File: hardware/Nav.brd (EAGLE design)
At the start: 47 x 40.5 mm, 52 parts

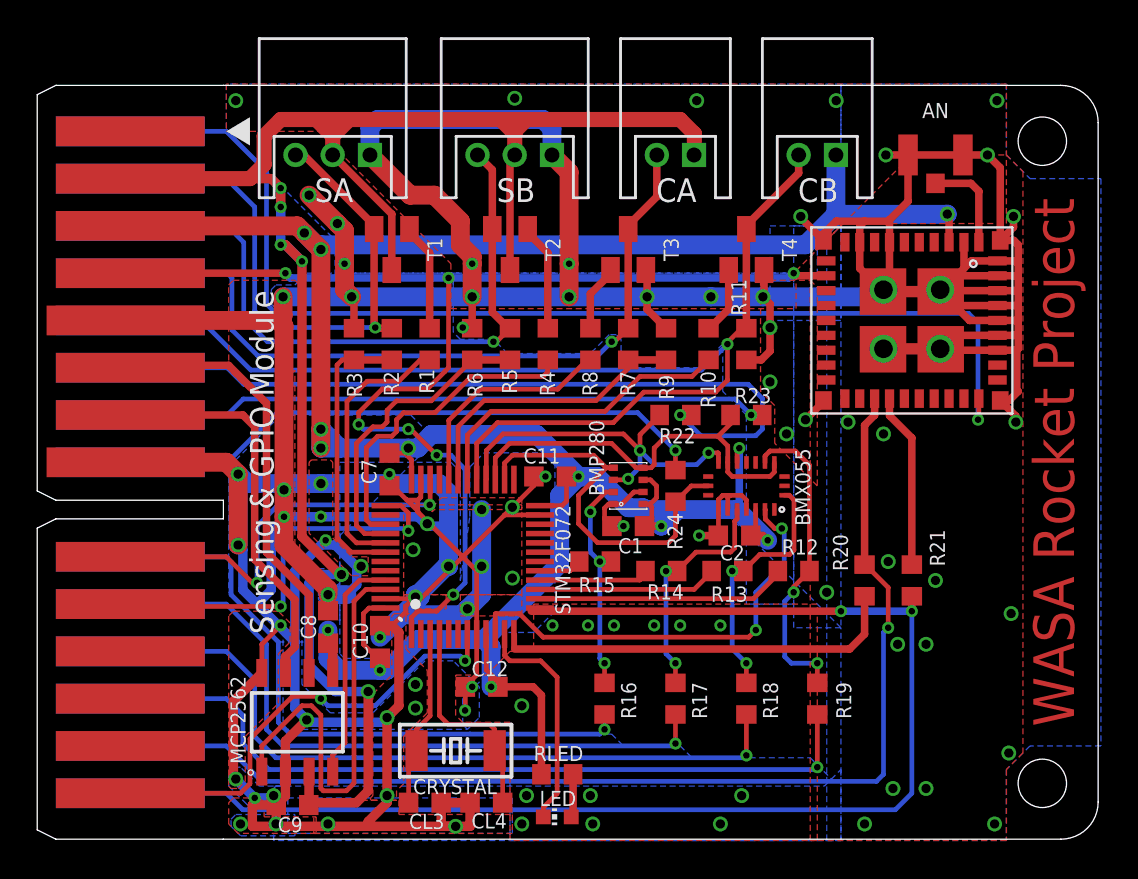
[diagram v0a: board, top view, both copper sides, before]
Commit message: Add nav board
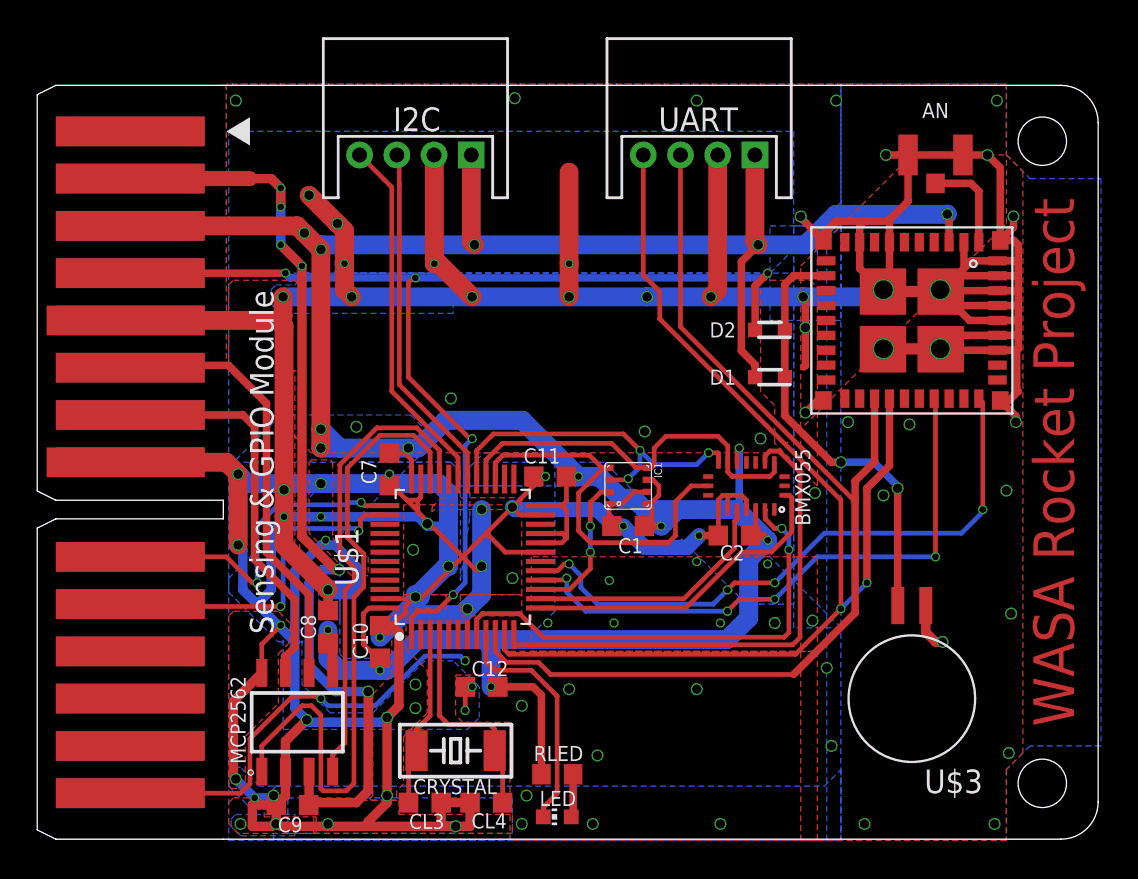
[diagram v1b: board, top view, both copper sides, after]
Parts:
- removed BMP280: BMP280, bosch-bmp280:BMP280
- removed CA, CB: (no value), jst-ph:S2B-PH-K-S
- removed R1, R10, R20, R21, R22, R23, R24, R4, R8: 1k, resistor:R0603
- removed R11, R16, R17, R18, R19, R2, R3, R5, R6, R7, R9: 10k, resistor:R0603
- removed R12, R13, R14, R15: 100k, resistor:R0603
- removed SA, SB: (no value), jst-ph:S3B-PH-K-S
- removed STM32F072: STM32F072-LQFP48, stm32f0:LQFP48
- removed T1, T2, T3, T4: (no value), transistor-neu-to92:SOT23-BEC
- added D1, D2: RB521S-30TE61, RB521S-30TE61:SODFL1608X70N
- added I2C, UART: (no value), jst-ph:S4B-PH-K-S
- added IC1: BME280, bosch-bme280:BME280
- added U$1: STM32G431-LQFP48, stm32g4:LQFP48
- added U$3: DCK-3R3E, capacitors:DC,DCK
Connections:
- removed net !HIL!: GYSFFMANC.32, U$2.16
- removed net CA: CA.2, R7.2, T3.C, U$2.19
- removed net CAI: R7.1, R9.2, STM32F072.31
- removed net CAO: R8.1, STM32F072.32
- removed net CB: CB.2, R11.2, STM32F072.29, T4.C, U$2.20
- removed net CBO: R10.1, STM32F072.30
- removed net N$10: R15.1, STM32F072.17
- removed net N$11: R20.1, STM32F072.12
- removed net N$12: GYSFFMANC.26, R21.2
- removed net N$13: R8.2, T3.B
- removed net N$14: R10.2, T4.B
- removed net N$15: R24.2, U$2.23
- removed net N$16: R23.2, U$2.22
- removed net N$17: R22.2, U$2.21
- removed net N$34: R19.2, U$2.28
- removed net N$35: R18.2, U$2.27
- removed net N$36: R17.2, U$2.26
- removed net N$43: R16.2, U$2.25
- removed net N$5: R1.2, T1.B
- removed net N$6: R4.2, T2.B
- removed net N$7: R13.1, STM32F072.15
- removed net N$8: R14.1, STM32F072.16
- removed net SA: R2.2, SA.3, T1.E, U$2.17
- removed net SAI: R2.1, R3.2, STM32F072.42
- removed net SAO: R1.1, STM32F072.41
- removed net SB: R5.2, SB.3, T2.E, U$2.18
- removed net SBI: R5.1, R6.2, STM32F072.40
- removed net SBO: R4.1, STM32F072.39
- new net N$3: GYSFFMANC.32, U$1.17
- new net SCL: I2C.4, U$1.31
- new net SDA: I2C.3, U$1.30
- new net VBACKUP: D1.1, D2.1, GYSFFMANC.14, U$3.+
- net !CS_ACCEL!: now also U$1.12; no longer R12.2, R19.1
- net !CS_GYRO!: now also U$1.14; no longer R14.2, R17.1
- net !CS_MAG!: now also U$1.13; no longer R13.2, R18.1
- net !CS_PRESS!: now also IC1.2, U$1.15; no longer BMP280.2, R15.2, R16.1
- net CAN_RX: now also U$1.33; no longer STM32F072.45
- net CAN_TX: now also U$1.34; no longer STM32F072.46
- net DRDYM: now also U$1.8; no longer STM32F072.10
- net GND: now also I2C.2, IC1.1, IC1.7, U$1.19, U$1.23, U$1.35, U$1.47, U$3.-, UART.2; no longer BMP280.1, BMP280.7, R11.1, R3.1, R6.1, R9.1, SA.1, SB.1, STM32F072.23, STM32F072.35, STM32F072.47, STM32F072.8, T3.E, T4.E
- net GPS_RX: now also GYSFFMANC.26, U$1.11, UART.4; no longer R21.1, STM32F072.13, U$2.30
- net GPS_TX: now also U$1.10, UART.3; no longer R20.2, U$2.29
- net MISO: now also IC1.5, U$1.28; no longer BMP280.5, R23.1, STM32F072.27
- net MOSI: now also IC1.3, U$1.29; no longer BMP280.3, R22.1, STM32F072.28
- net N$2: now also GYSFFMANC.29, U$1.16; no longer R12.1, STM32F072.14
- net N$51: now also U$1.9; no longer STM32F072.11
- net N$70: now also U$1.4; no longer STM32F072.4
- net N$71: now also U$1.3; no longer STM32F072.3
- net NRST1: no longer STM32F072.7
- net SCK: now also IC1.4, U$1.27; no longer BMP280.4, R24.1, STM32F072.26
- net SWCLK1: now also U$1.38; no longer STM32F072.37
- net SWDIO1: now also U$1.37; no longer STM32F072.34
- net VBAT: now also D2.2, U$1.1; no longer GYSFFMANC.14, STM32F072.1
- net VCC: no longer CA.1, SA.2, SB.2, T1.C, T2.C
- net VDD: now also D1.2, I2C.1, IC1.6, IC1.8, U$1.20, U$1.21, U$1.24, U$1.36, U$1.48, UART.1; no longer BMP280.6, BMP280.8, CB.1, STM32F072.24, STM32F072.36, STM32F072.48, STM32F072.9
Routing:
- net CB: track 64.4 -> 0.00 mm, vias 1 -> 0
- net !HIL!: track 60.3 -> 0.00 mm, vias 1 -> 0
- net VCC: track 102.3 -> 53.6 mm
- net N$34: track 42.3 -> 0.00 mm, vias 1 -> 0
- net N$17: track 42.1 -> 0.00 mm, vias 1 -> 0
- net CA: track 40.8 -> 0.00 mm, vias 1 -> 0
- net N$35: track 39.5 -> 0.00 mm, vias 1 -> 0
- net N$36: track 36.7 -> 0.00 mm, vias 1 -> 0
- net SB: track 35.7 -> 0.00 mm, vias 1 -> 0
- net N$16: track 34.7 -> 0.00 mm, vias 1 -> 0
- net N$43: track 33.9 -> 0.00 mm, vias 1 -> 0
- net N$3: track 0.00 -> 33.4 mm, vias 0 -> 4
- net N$15: track 32.3 -> 0.00 mm, vias 1 -> 0
- net SA: track 32.0 -> 0.00 mm, vias 1 -> 0
- net VDD: track 153.1 -> 178.1 mm, vias 13 -> 15
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
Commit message: Fix reset wire
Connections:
- removed net NRST1: U$2.15
- new net N$4: U$1.7, U$2.15
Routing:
- net NRST1: track 23.2 -> 0.00 mm, vias 2 -> 0
- net N$4: track 0.00 -> 23.2 mm, vias 0 -> 2
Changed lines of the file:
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@@
 <wire x1="17.53385" y1="-4.910653125" x2="17.53385" y2="-6.703" width="0.254" layer="1"/>
-</signal>
-<signal name="NRST1">
-<contactref element="U$2" pad="15"/>
-<wire x1="22.987" y1="-10.668" x2="23.11" y2="-10.545" width="0.254" layer="1"/>
-<via x="22.987" y="-10.668" extent="1-16" drill="0.35"/>
-<wire x1="5" y1="-17.78" x2="10.922" y2="-17.78" width="0.254" layer="1"/>
-<wire x1="22.987" y1="-10.668" x2="22.733" y2="-10.414" width="0.254" layer="16"/>
-<wire x1="22.733" y1="-10.414" x2="20.828" y2="-10.414" width="0.254" layer="16"/>
-<via x="15.24" y="-12.7" extent="1-16" drill="0.35"/>
-<wire x1="10.922" y1="-17.78" x2="11.43" y2="-17.272" width="0.254" layer="1"/>
-<wire x1="20.828" y1="-10.414" x2="18.161" y2="-13.081" width="0.254" layer="16"/>
-<wire x1="18.161" y1="-13.081" x2="15.621" y2="-13.081" width="0.254" layer="16"/>
-<wire x1="15.621" y1="-13.081" x2="15.24" y2="-12.7" width="0.254" layer="16"/>
-<wire x1="11.43" y1="-14.859" x2="13.716" y2="-12.573" width="0.254" layer="1"/>
-<wire x1="15.113" y1="-12.573" x2="13.716" y2="-12.573" width="0.254" layer="1"/>
-<wire x1="15.113" y1="-12.573" x2="15.24" y2="-12.7" width="0.254" layer="1"/>
-<wire x1="11.43" y1="-17.272" x2="11.43" y2="-14.859" width="0.254" layer="1"/>
 </signal>
 <signal name="DRDYM">
@@
 <wire x1="50.8" y1="3.21" x2="50.8" y2="-2.54" width="0.254" layer="1"/>
 </signal>
+<signal name="N$4">
+<contactref element="U$1" pad="7"/>
+<contactref element="U$2" pad="15"/>
+<wire x1="22.987" y1="-10.668" x2="23.11" y2="-10.545" width="0.254" layer="1"/>
+<via x="22.987" y="-10.668" extent="1-16" drill="0.35"/>
+<wire x1="5" y1="-17.78" x2="10.922" y2="-17.78" width="0.254" layer="1"/>
+<wire x1="22.987" y1="-10.668" x2="22.733" y2="-10.414" width="0.254" layer="16"/>
+<wire x1="22.733" y1="-10.414" x2="20.828" y2="-10.414" width="0.254" layer="16"/>
+<via x="15.24" y="-12.7" extent="1-16" drill="0.35"/>
+<wire x1="10.922" y1="-17.78" x2="11.43" y2="-17.272" width="0.254" layer="1"/>
+<wire x1="20.828" y1="-10.414" x2="18.161" y2="-13.081" width="0.254" layer="16"/>
+<wire x1="18.161" y1="-13.081" x2="15.621" y2="-13.081" width="0.254" layer="16"/>
+<wire x1="15.621" y1="-13.081" x2="15.24" y2="-12.7" width="0.254" layer="16"/>
+<wire x1="11.43" y1="-14.859" x2="13.716" y2="-12.573" width="0.254" layer="1"/>
+<wire x1="15.113" y1="-12.573" x2="13.716" y2="-12.573" width="0.254" layer="1"/>
+<wire x1="15.113" y1="-12.573" x2="15.24" y2="-12.7" width="0.254" layer="1"/>
+<wire x1="11.43" y1="-17.272" x2="11.43" y2="-14.859" width="0.254" layer="1"/>
+<wire x1="23.11" y1="-10.545" x2="23.11" y2="-9.2583" width="0" layer="19" extent="1-1"/>
+</signal>
 </signals>
